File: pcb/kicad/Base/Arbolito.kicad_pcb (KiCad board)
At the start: 2 copper layers, 73 x 66 mm, 72 parts, among them J1 Battery, J10 Conn_01x01, J11 Conn_01x01, J12 Conn_01x01, J13 Conn_01x01, J14 Conn_01x01, J2 Conn_01x06_Female, J3 Conn_01x01, J4 Conn_01x01, J5 Conn_01x01, J6 Conn_01x01, J7 Conn_01x01, J8 Conn_01x01, J9 Conn_01x01, Q1 S8050, Q2 S8050, Q3 S8050, SW1 SW_DP3T, SW2 SW_Push, SW3 SW_Push, SW4 SW_Push, U1 NCP115AMX120TCG, U2 CH340C, U3 AP63205WU, U4 ESP-12F, U5 SHT31-DIS

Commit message: idk
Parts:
- C11, C12, C4: value 0.1uF -> 100n
- renumbered Pe to P1
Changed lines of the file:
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@@
         (effects (font (size 1 1) (thickness 0.15)))
     )
-    (fp_text value "0.1uF" (at 0 1.68 90) (layer "F.Fab")
+    (fp_text value "100n" (at 0 1.68 90) (layer "F.Fab")
         (effects (font (size 1 1) (thickness 0.15)))
     )
@@
     (property "Sheetfile" "Arbolito.kicad_sch")
     (property "Sheetname" "")
+    (property "dnp" "")
     (property "ki_description" "Resistor")
     (property "ki_keywords" "R res resistor")
@@
     (descr "Sensirion DFN-8 SHT3x-DIS (https://www.sensirion.com/fileadmin/user_upload/customers/sensirion/Dokumente/2_Humidity_Sensors/Datasheets/Sensirion_Humidity_Sensors_SHT3x_Datasheet_digital.pdf)")
     (tags "sensirion dfn nolead")
+    (property "Field5" "")
     (property "Sheetfile" "Arbolito.kicad_sch")
     (property "Sheetname" "")
+    (property "dnp" "")
     (property "ki_description" "I²C humidity and temperature sensor, ±2%RH, ±0.2°C, DFN-8")
     (property "ki_keywords" "digital temperature humidity i2c")
@@
     (property "Sheetfile" "Arbolito.kicad_sch")
     (property "Sheetname" "")
+    (property "dnp" "")
     (property "ki_description" "Resistor")
     (property "ki_keywords" "R res resistor")
@@
     (property "ki_keywords" "usb universal serial bus type-C USB2.0")
     (attr smd)
-    (fp_text reference "Pe" (at 0 -4.58 90) (layer "F.SilkS")
+    (fp_text reference "P1" (at 0 -4.58 90) (layer "F.SilkS")
         (effects (font (size 1 1) (thickness 0.15)))
     )
@@
     (property "Sheetfile" "Arbolito.kicad_sch")
     (property "Sheetname" "")
+    (property "dnp" "")
     (property "ki_description" "Unpolarized capacitor")
     (property "ki_keywords" "cap capacitor")
@@
         (effects (font (size 1 1) (thickness 0.15)))
     )
-    (fp_text value "0.1uF" (at 0 1.68) (layer "F.Fab")
+    (fp_text value "100n" (at 0 1.68) (layer "F.Fab")
         (effects (font (size 1 1) (thickness 0.15)))
     )
@@
         (effects (font (size 1 1) (thickness 0.15)))
     )
-    (fp_text value "0.1uF" (at 0 1.68) (layer "F.Fab")
+    (fp_text value "100n" (at 0 1.68) (layer "F.Fab")
         (effects (font (size 1 1) (thickness 0.15)))
     )

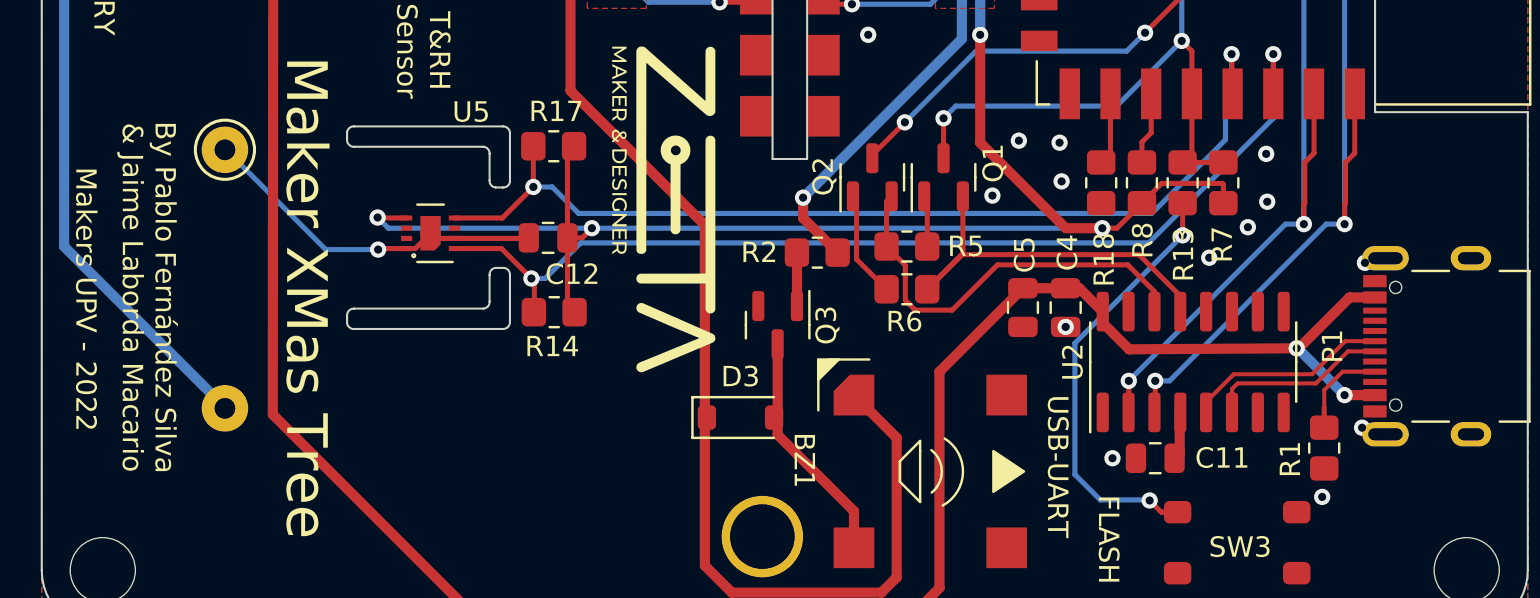
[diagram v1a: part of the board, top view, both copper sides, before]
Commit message: USB Issues fixed
USB C Now reversible
USB C progamable
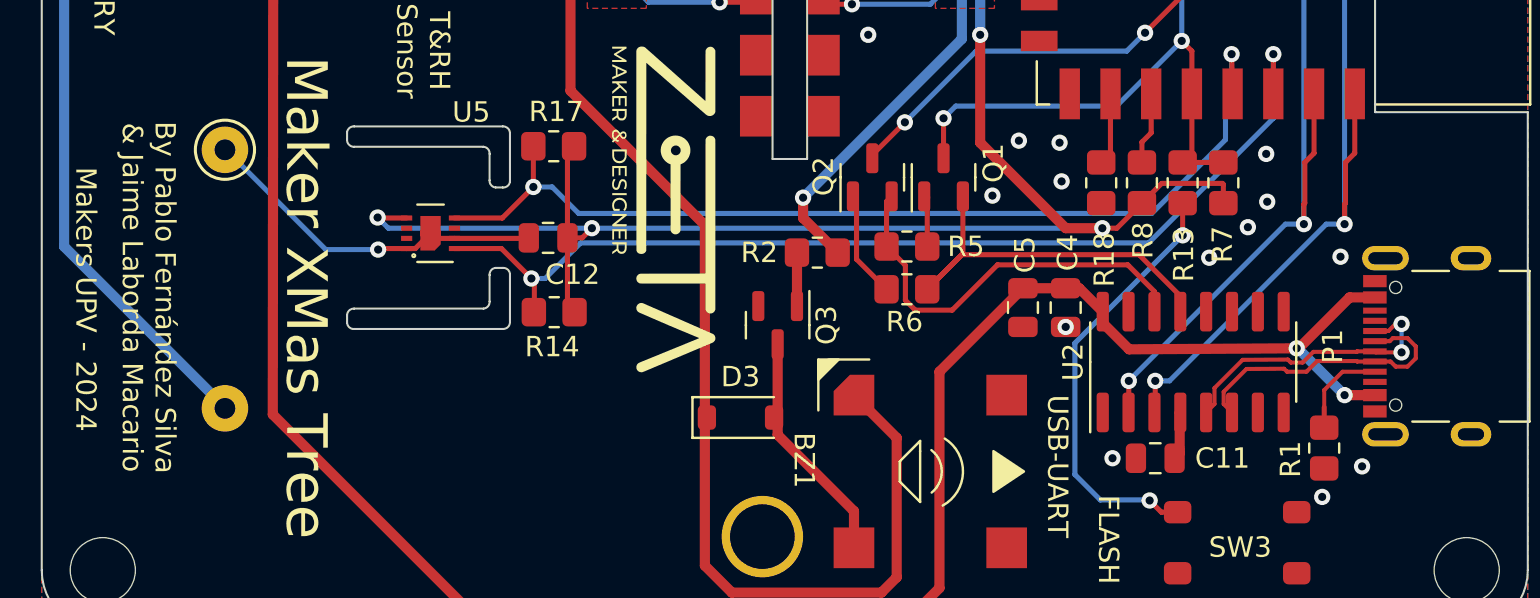
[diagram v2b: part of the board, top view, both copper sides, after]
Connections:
- P1 pad B6: (no net) -> /D+
- P1 pad B7: (no net) -> /D-
- U2 pad 5: /D- -> /D+
- U2 pad 6: /D+ -> /D-
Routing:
- net /D+: track 8.94 -> 14.3 mm, vias 0 -> 2
- net /D-: track 9.53 -> 14.5 mm
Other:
- board text added: "Makers UPV - 2024"
- board text removed: "Makers UPV - 2022"
